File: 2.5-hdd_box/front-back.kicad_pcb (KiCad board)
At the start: 2 copper layers, 102 x 24 mm, 8 parts

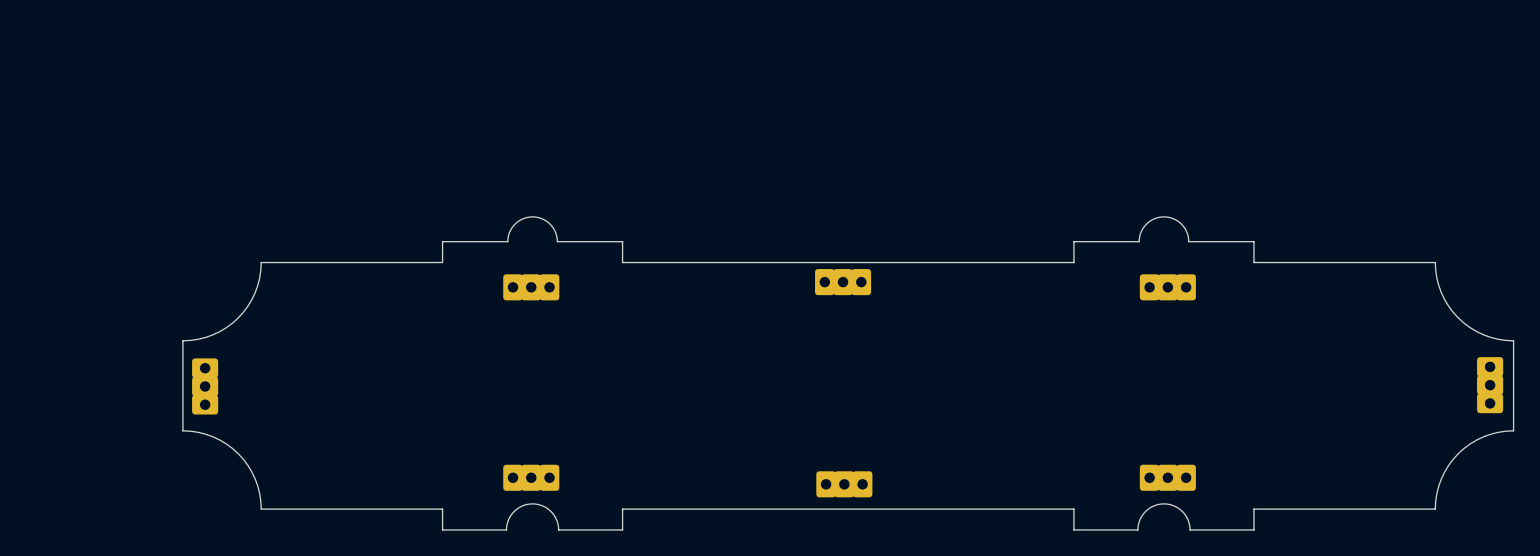
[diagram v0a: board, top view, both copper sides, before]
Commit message: 2.5-hdd_box: cut on bottom for usb-sata board, better placement of soldier pads
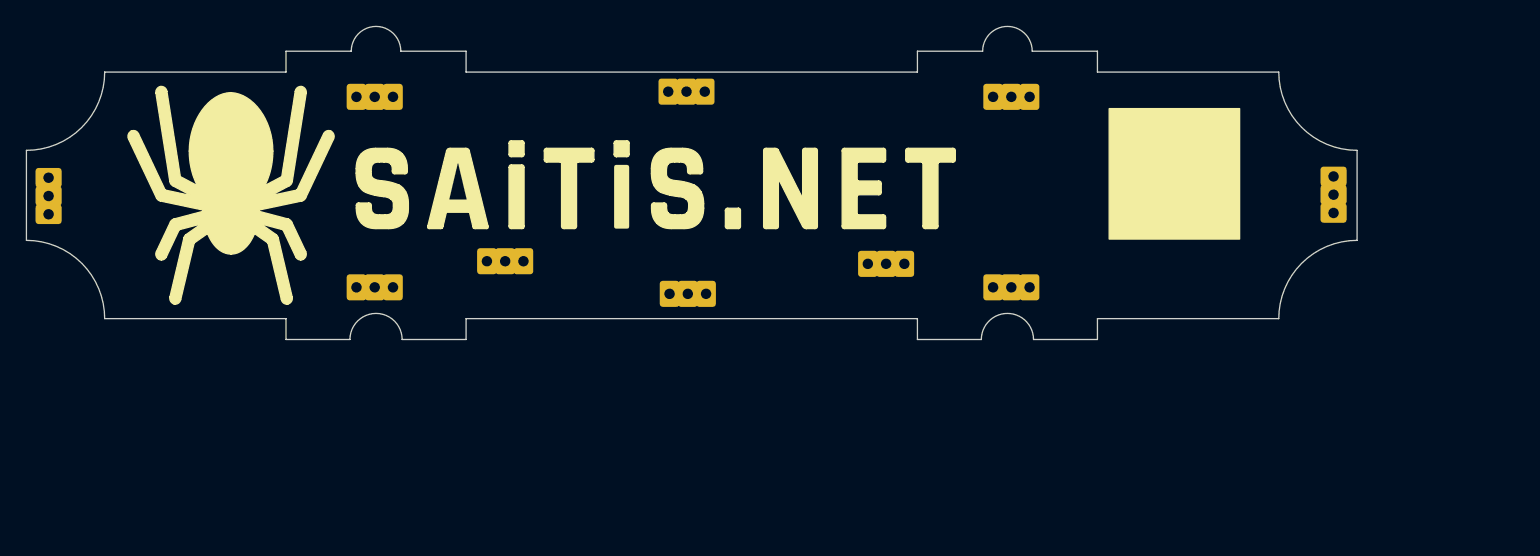
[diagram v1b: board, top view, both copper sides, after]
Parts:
- removed the REF** at (83.8, 87.3)
- removed the REF** at (83.8, 72.7)
- removed the REF** at (132.6, 72.7)
- removed the REF** at (107.8, 87.8)
- removed the REF** at (157.2, 80.3)
- removed the REF** at (58.7, 80.4)
- removed the REF** at (107.7, 72.3)
- removed the REF** at (132.6, 87.3)
- added REF**: soldpad, Local:soldpad, F.Cu at (145.2, 65.7)
- added REF**: soldpad, Local:soldpad, F.Cu at (95.8, 73.2)
- added REF**: soldpad, Local:soldpad, F.Cu at (46.7, 65.8)
- added REF**: soldpad, Local:soldpad, F.Cu at (71.8, 58.1)
- added REF**: soldpad, Local:soldpad, F.Cu at (71.8, 72.7)
- added REF**: soldpad, Local:soldpad, F.Cu at (95.7, 57.7)
- added REF**: soldpad, Local:soldpad, F.Cu at (120.6, 58.1)
- added REF**: soldpad, Local:soldpad, F.Cu at (120.6, 72.7)
- added REF**: soldpad, Local:soldpad, F.Cu at (111.0, 70.9)
- added REF**: soldpad, Local:soldpad, F.Cu at (81.8, 70.7)

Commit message: last order has small mistakes, this one should be better. Other things added, your responsibility to discover
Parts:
- removed the REF** at (145.2, 65.7)
- removed the REF** at (46.7, 65.8)
- removed the REF** at (111.0, 70.9)
- removed the REF** at (81.8, 70.7)
- added REF**: soldpad, Local:soldpad, B.Cu at (46.6, 66.5)
- added REF**: soldpad, Local:soldpad, B.Cu at (145.4, 66.6)
- REF** (x6): moved to B.Cu
- turned REF** to 180 degrees (x6)
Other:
- board size 102 x 24 mm -> 102 x 23.3 mm
